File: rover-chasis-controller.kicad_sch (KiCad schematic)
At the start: 70 parts, among them J1 Motor control, J11 Compass Connection (I2C), J15 External LED (Red), J16 External LED (Yellow), J17 External LED (Green), J2 Motor control, J22 Ultrasonic Sensor Inputs, J3 Motor control, J38 Motor control, J4 Screw_Terminal_01x02, J40 Encoder, J41 Encoder, J42 Encoder, J43 Encoder, J7 TTL, J8 Ultrasonic Sensor Inputs, Q2 HSBA100P04_C2987717, U1 APT2012LVBC/D, U2 APT2012LVBC/D, U3 APT2012LVBC/D, U4 AP64500, U5 MPU-6050_C24112, U6 PCA9685PW,118, U7 APT2012LVBC/D

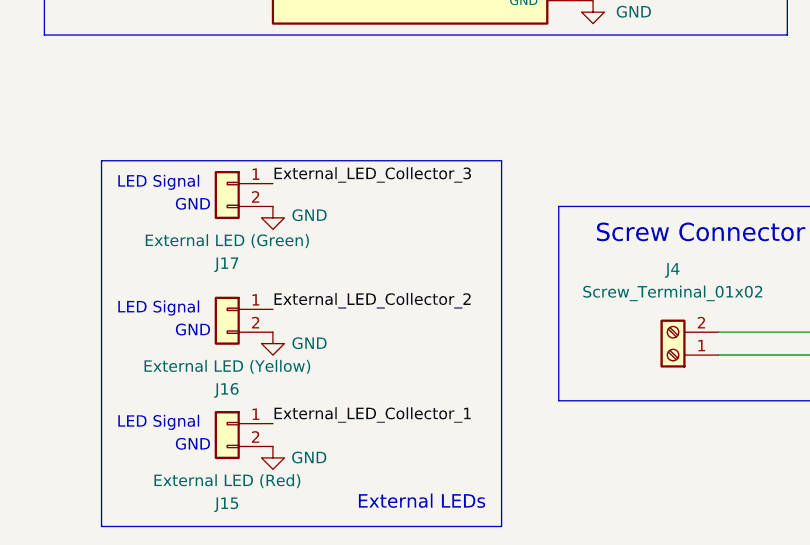
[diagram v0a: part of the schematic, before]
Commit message: Issue #1: Corrected some mistakes
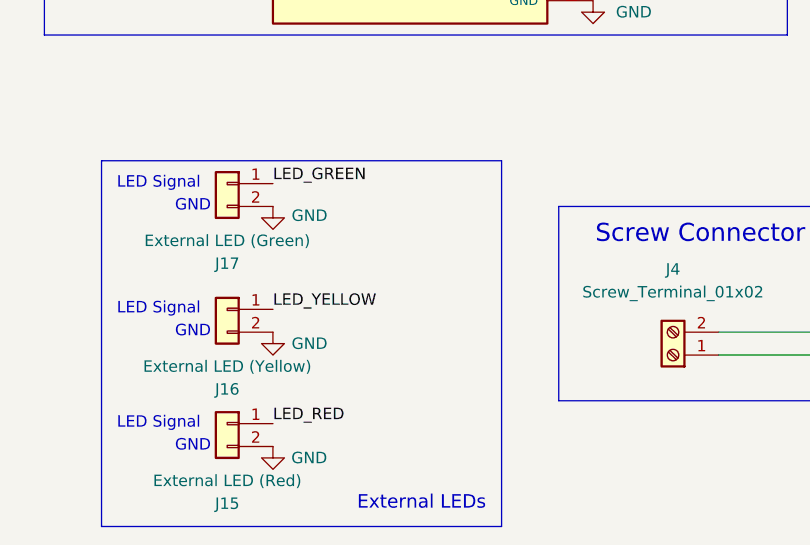
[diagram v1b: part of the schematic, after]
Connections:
- net External_LED_Collector_1 is gone; now on net LED_RED: J15.1 (Pin_1)
- net External_LED_Collector_2 is gone; now on net LED_YELLOW: J16.1 (Pin_1)
- net External_LED_Collector_3 is gone; now on net LED_GREEN: J17.1 (Pin_1)
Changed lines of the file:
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@@
 		)
 	)
-	(label "External_LED_Collector_2"
+	(label "LED_YELLOW"
 		(at 41.91 212.09 0)
 		(effects
@@
 		)
 	)
-	(label "External_LED_Collector_1"
+	(label "LED_RED"
 		(at 41.91 224.79 0)
 		(effects
@@
 		)
 	)
-	(label "External_LED_Collector_3"
+	(label "LED_GREEN"
 		(at 41.91 198.12 0)
 		(effects

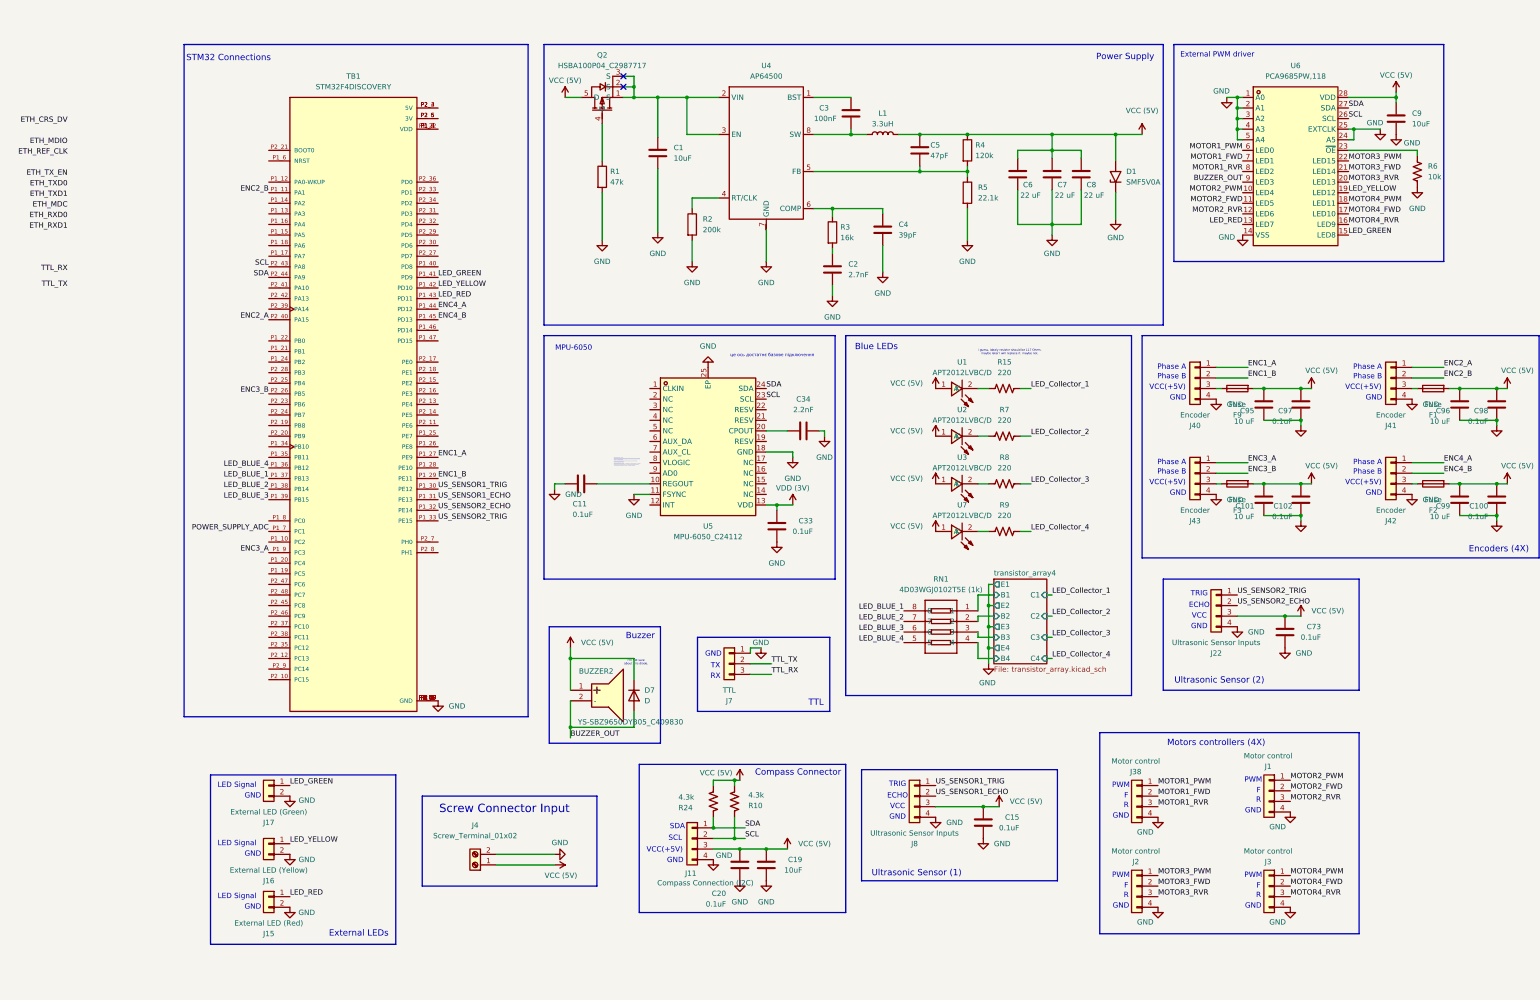
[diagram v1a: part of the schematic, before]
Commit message: Issue #1: Corrected some mistakes
Solved short circuit problems, replaced components smaller that 0805, adjusted references on the pcb design, connected TTL connector to STM32, added missing schematic to measure input voltage
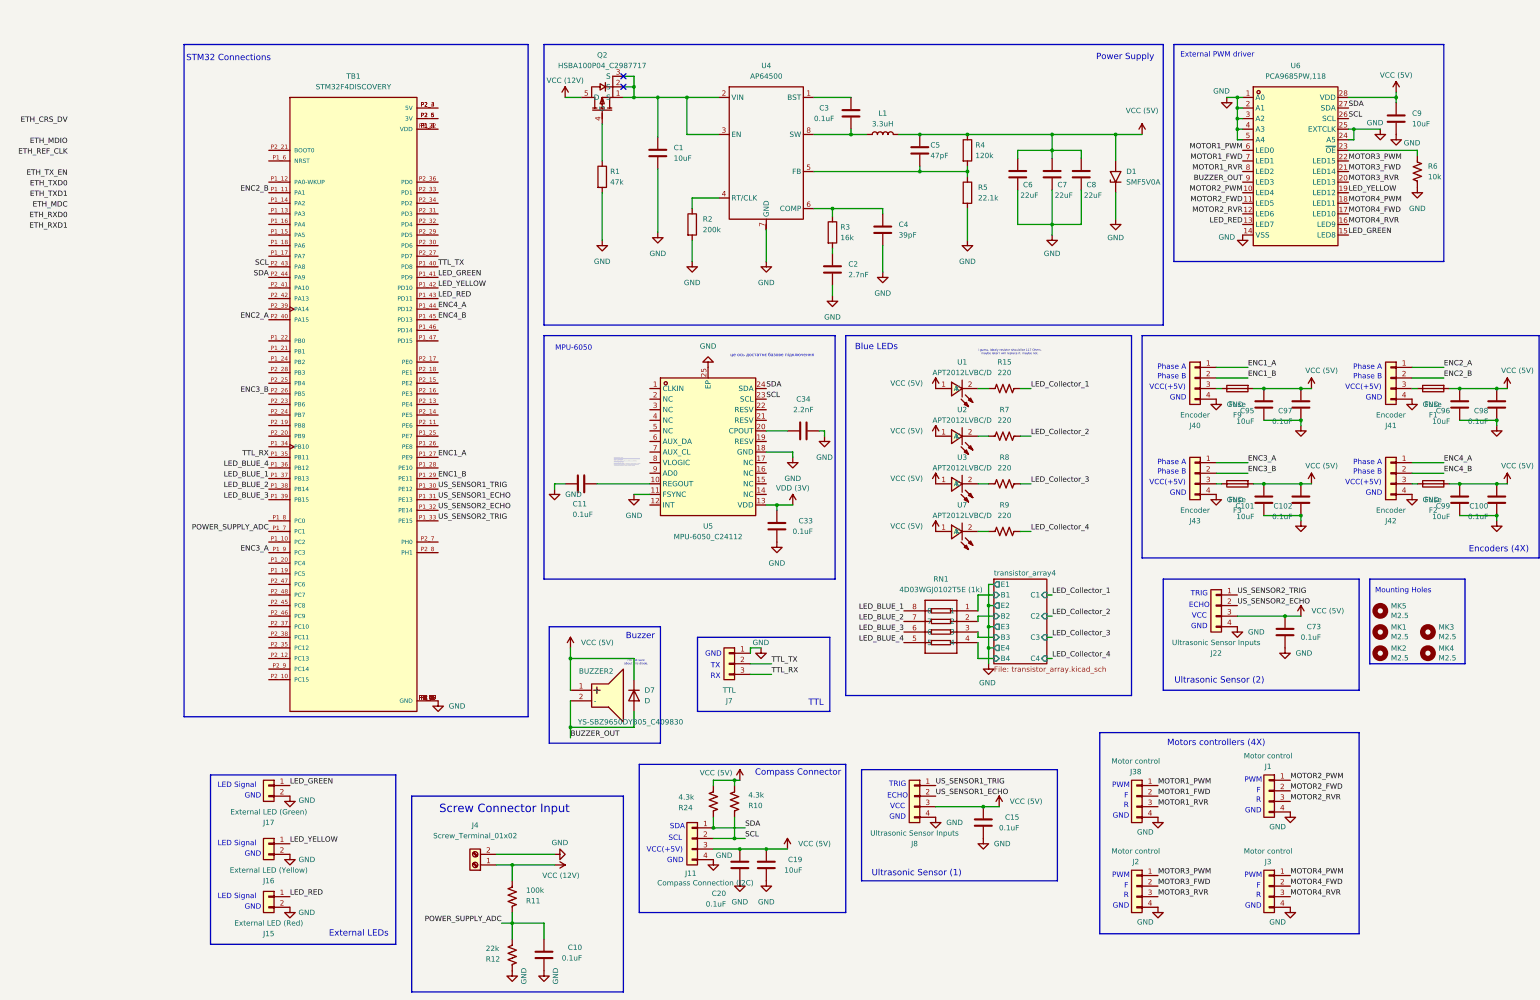
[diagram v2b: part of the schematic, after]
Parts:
- added C10: 0.1uF, Capacitor_SMD:C_0805_2012Metric, symbol Device:C
- added MK1, MK2, MK3, MK4, MK5: M2.5, MountingHole:MountingHole_2.7mm_M2.5_Pad, symbol Mechanical:MountingHole
- added R11: 100k, Resistor_SMD:R_0805_2012Metric, symbol Device:R_US
- added R12: 22k, Resistor_SMD:R_0805_2012Metric, symbol Device:R_US
- C1, C9: LCSC Part (none) -> C1713
- C100, C102, C20, C33, C73, C97, C98: footprint Capacitor_SMD:C_0603_1608Metric -> Capacitor_SMD:C_0805_2012Metric; LCSC Part C14663 -> C49678
- C101, C95, C96, C99: value 10 uF -> 10uF
- C11, C15: footprint Capacitor_SMD:C_0603_1608Metric -> Capacitor_SMD:C_0805_2012Metric; LCSC https://www.lcsc.com/product-detail/Multilayer-Ceramic-Capa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 -> (none); LCSC Part C14663 -> C49678
- C2: LCSC Part (none) -> C2918070
- C3: value 100nF -> 0.1uF; LCSC Part (none) -> C49678
- C34: footprint Capacitor_SMD:C_01005_0402Metric -> Capacitor_SMD:C_0805_2012Metric; LCSC https://www.lcsc.com/product-detail/Multilayer-Ceramic-Capa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 -> (none); LCSC Part C106861 -> C28260
- C4: LCSC Part (none) -> C576897
- C5: LCSC Part (none) -> C113821
- C6, C7, C8: value 22 uF -> 22uF; LCSC Part (none) -> C87996
- D1: LCSC Part (none) -> C42387343
- J4: LCSC Part (none) -> C3018698
- L1: LCSC Part (none) -> C7587741
- Q2: LCSC Part (none) -> C2987717
- R1: LCSC Part (none) -> C2989281
- R10, R24: footprint Resistor_SMD:R_0402_1005Metric -> Resistor_SMD:R_1206_3216Metric; LCSC Part C112291 -> C2933704
- R15, R7, R8, R9: footprint Resistor_SMD:R_0402_1005Metric -> Resistor_SMD:R_0805_2012Metric; LCSC Part C112291 -> C17557
- R2: LCSC Part (none) -> C728645
- R3: LCSC Part (none) -> C865809
- R4: LCSC Part (none) -> C103948
- R5: LCSC Part (none) -> C2692772
- R6: footprint Resistor_SMD:R_0402_1005Metric -> Resistor_SMD:R_0805_2012Metric; LCSC Part C60490 -> C17414
- U4: LCSC Part (none) -> C2070920
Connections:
- net GND: now also C10.1, R12.2
- net POWER_SUPPLY_ADC: now also C10.2, R11.2, R12.1
- net TTL_RX: now also TB1.P1_35 (PB11)
- net TTL_TX: now also TB1.P1_40 (PD8)
- net VCC (5V): no longer J4.1 (Pin_1), Q2.5 (D)
- new net VCC (12V): J4.1 (Pin_1), Q2.5 (D), R11.1
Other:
- note added: "Mounting Holes"

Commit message: Issue #1: Prepare for production
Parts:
- added J17, J32: Conn_02x25_Counter_Clockwise, symbol Connector_Generic:Conn_02x25_Counter_Clockwise
- added J18, J19, J20, J21, J22, J27, J28, J29, J30, J31: Conn_01x04, symbol Connector_Generic:Conn_01x04
- added J23: Conn_01x03, symbol Connector_Generic:Conn_01x03
- added J24, J25, J26: Conn_01x02, symbol Connector_Generic:Conn_01x02
- C16: renamed from C95; value 10uF -> 10uFx16V; LCSC Part C1713 -> C18185764
- C17: renamed from C101; value 10uF -> 10uFx16V; LCSC Part C1713 -> C18185764
- C21: renamed from C9; value 10uF -> 10uFx16V; footprint Capacitor_SMD:C_1206_3216Metric -> Capacitor_SMD:C_0805_2012Metric; LCSC C13585 -> C18185764; LCSC Part C1713 -> C18185764
- C22: renamed from C96; value 10uF -> 10uFx16V; LCSC Part C1713 -> C18185764
- C23: renamed from C99; value 10uF -> 10uFx16V; LCSC Part C1713 -> C18185764
- C3: renamed from C1; value 10uF -> 10uFx50V; LCSC C13585 -> C513774; LCSC Part C1713 -> C513774
- C5: renamed from C19; value 10uF -> 10uFx16V; LCSC Part C1713 -> C18185764
- C7: renamed from C34; LCSC Part C28260 -> C107146
- J1: renamed from J17; LCSC Part C495693 -> C131337
- J10: renamed from J40; LCSC Part C111514 -> C131334
- J11: renamed from J43; LCSC Part C111514 -> C131334
- J12: renamed from J22; LCSC Part C111514 -> C131334
- J13: renamed from J1; LCSC Part C111514 -> C131334
- J14: renamed from J3; LCSC Part C111514 -> C131334
- J15: renamed from J41; LCSC Part C111514 -> C131334
- J16: renamed from J42; LCSC Part C111514 -> C131334
- J2: renamed from J16; LCSC Part C495693 -> C131337
- J3: renamed from J15; LCSC Part C495693 -> C131337
- J5: renamed from J11; LCSC Part C111514 -> C131334
- J6: renamed from J7; LCSC Part C265393 -> C131339
- J7: renamed from J8; LCSC Part C111514 -> C131334
- J8: renamed from J38; LCSC Part C111514 -> C131334
- J9: renamed from J2; LCSC Part C111514 -> C131334
- R5: renamed from R24; footprint Resistor_SMD:R_1206_3216Metric -> Resistor_SMD:R_0805_2012Metric; LCSC Part C2933704 -> C728653
- R6: renamed from R10; footprint Resistor_SMD:R_1206_3216Metric -> Resistor_SMD:R_0805_2012Metric; LCSC Part C2933704 -> C728653
- TB1: LCSC Part C118360 -> (none)
- U3: renamed from U1; LCSC Part C5879383 -> C965817
- U4: renamed from U2; LCSC Part C5879383 -> C965817
- U5: renamed from U3; LCSC Part C5879383 -> C965817
- U6: renamed from U7; LCSC Part C5879383 -> C965817
- renumbered BUZZER2 to BUZZER1, C10 to C1, C4 to C10, C5 to C11, C15 to C12, C6 to C13, C7 to C14, C8 to C15, C73 to C18, C97 to C19, C11 to C2, C102 to C20, C98 to C24, C100 to C25, C20 to C4, C33 to C6, C2 to C8, C3 to C9, D7 to D1, D1 to D2, F9 to F1, F3 to F2, F1 to F3, F2 to F4, MK5 to MK1, MK1 to MK2, MK2 to MK3, MK3 to MK4, MK4 to MK5, Q2 to Q1, R11 to R1, R15 to R10, R7 to R11, R8 to R12, R9 to R13, R6 to R14, R12 to R2, R1 to R3, R2 to R4, R3 to R7, R4 to R8, R5 to R9, U5 to U1, U4 to U2, U6 to U7
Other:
- note removed: "TODO: 7. Resolve all ERC exceptions and warnings. 9. Recalculate all of the numerical values for scheme, to be sure. 13. Consider implement Multi unit symbols for IC Arrays. 15. Include PWR_FLAG, properly. DONE: 1. Rework transisor schemes with transistor arrays. 1.1 Motor controllers. 1.2 External LEDs. 1.3 Buzzer. 2. Rework power supply by taking already in use PMIC in rpi-power-HAT. (Varya PCB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"
- note removed: "Коли використовувати VLOGIC: Якщо ви підключаєте MPU-6050 до мікроконтролера, який працює на логічних рівнях 1.8В або 5В, тоді ви можете використовувати VLOGIC для встановлення рівнів логіки, сумісних із мікроконтролером. VLOGIC дозволяє забезпечити сумісність між рівнями сигналів I2C (SDA/SCL) і рівнями GPIO мікроконтролера. Коли можна обійтися без VLOGIC: Якщо ваш STM32 працює на 3.3В, як і сам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"
- company: (none) -> KPI Rover
- title: Rover Chassis Controller PCB -> Chassis Controller
- moved on the sheet: C1, C12, C4, C5, J13, J14, J4, J5, J6, J7, J8, J9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
